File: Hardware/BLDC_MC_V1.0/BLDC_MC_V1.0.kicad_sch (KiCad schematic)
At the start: 0 parts

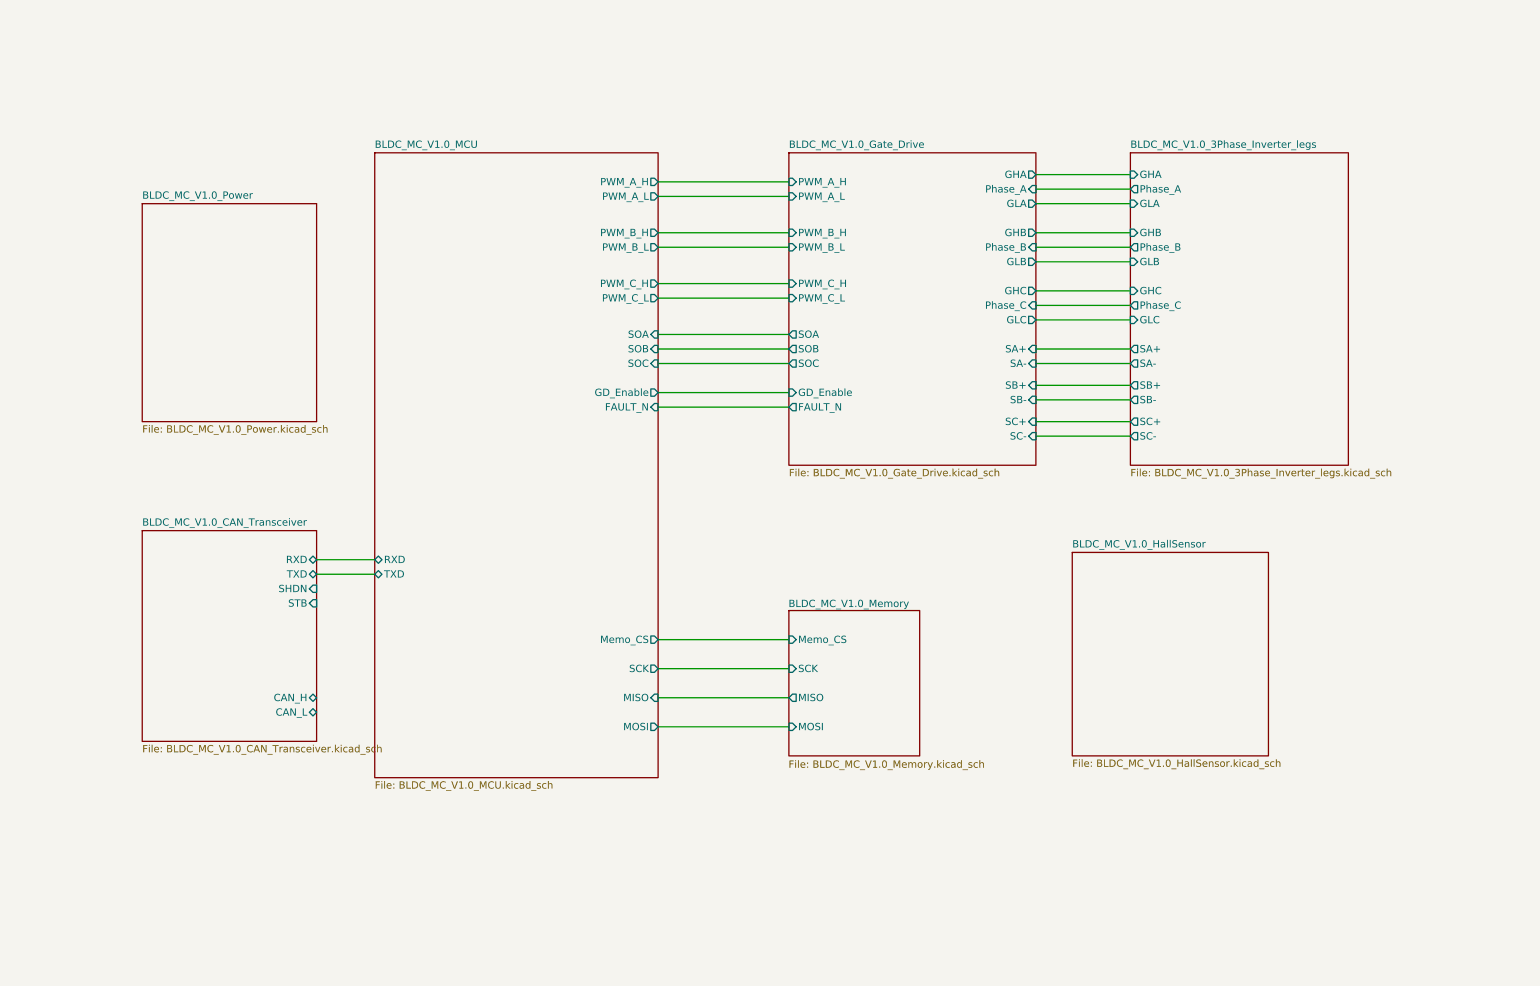
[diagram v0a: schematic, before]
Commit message: Edit the sch of the project by adding the hall sensor sheet and interface with the MCU sheet and annotate the components in memory sheet
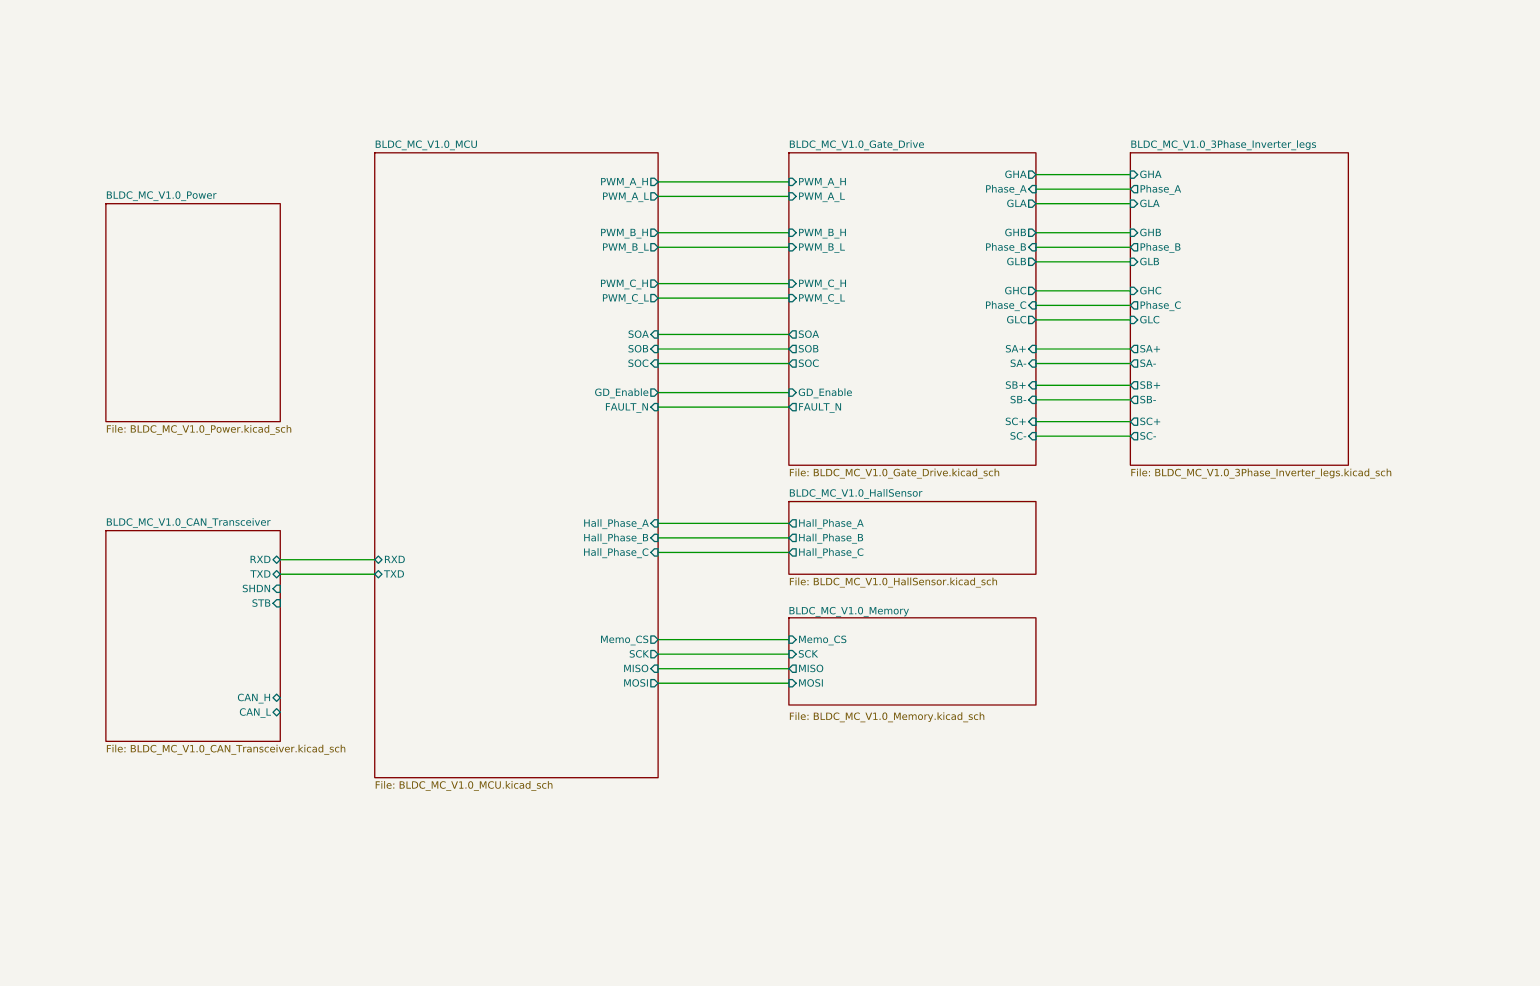
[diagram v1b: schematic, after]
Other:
- sheet BLDC_MC_V1.0_HallSensor ports: added Hall_Phase_A, Hall_Phase_B, Hall_Phase_C; removed none
- sheet BLDC_MC_V1.0_MCU ports: added Hall_Phase_A, Hall_Phase_B, Hall_Phase_C; removed none
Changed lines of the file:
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@@
 	(wire
 		(pts
-			(xy 77.47 115.57) (xy 87.63 115.57)
+			(xy 137.16 134.62) (xy 160.02 134.62)
+		)
+		(stroke
+			(width 0)
+			(type default)
+		)
+	)
+	(wire
+		(pts
+			(xy 137.16 111.76) (xy 160.02 111.76)
+		)
+		(stroke
+			(width 0)
+			(type default)
+		)
+	)
+	(wire
+		(pts
+			(xy 71.12 115.57) (xy 87.63 115.57)
 		)
 		(stroke
@@
 	(wire
 		(pts
-			(xy 77.47 118.11) (xy 87.63 118.11)
+			(xy 71.12 118.11) (xy 87.63 118.11)
 		)
 		(stroke
@@
 	(wire
 		(pts
-			(xy 137.16 134.62) (xy 160.02 134.62)
-		)
-		(stroke
-			(width 0)
-			(type default)
-		)
-	)
-	(wire
-		(pts
 			(xy 203.2 68.58) (xy 219.71 68.58)
 		)
@@
 	(wire
 		(pts
+			(xy 137.16 132.08) (xy 160.02 132.08)
+		)
+		(stroke
+			(width 0)
+			(type default)
+		)
+	)
+	(wire
+		(pts
 			(xy 203.2 93.98) (xy 219.71 93.98)
 		)
@@
 	(wire
 		(pts
+			(xy 137.16 109.22) (xy 160.02 109.22)
+		)
+		(stroke
+			(width 0)
+			(type default)
+		)
+	)
+	(wire
+		(pts
 			(xy 137.16 60.96) (xy 160.02 60.96)
 		)
@@
 	(wire
 		(pts
+			(xy 137.16 129.54) (xy 160.02 129.54)
+		)
+		(stroke
+			(width 0)
+			(type default)
+		)
+	)
+	(wire
+		(pts
 			(xy 203.2 78.74) (xy 219.71 78.74)
 		)
@@
 	(wire
 		(pts
-			(xy 137.16 144.78) (xy 160.02 144.78)
-		)
-		(stroke
-			(width 0)
-			(type default)
-		)
-	)
-	(wire
-		(pts
-			(xy 137.16 139.7) (xy 160.02 139.7)
+			(xy 137.16 114.3) (xy 160.02 114.3)
 		)
 		(stroke
@@
 	(wire
 		(pts
+			(xy 137.16 137.16) (xy 160.02 137.16)
+		)
+		(stroke
+			(width 0)
+			(type default)
+		)
+	)
+	(wire
+		(pts
 			(xy 137.16 52.07) (xy 160.02 52.07)
 		)
@@
 	(wire
 		(pts
-			(xy 137.16 129.54) (xy 160.02 129.54)
-		)
-		(stroke
-			(width 0)
-			(type default)
-		)
-	)
-	(wire
-		(pts
 			(xy 203.2 58.42) (xy 219.71 58.42)
 		)
@@
 	)
 	(sheet
-		(at 46.99 110.49)
+		(at 40.64 110.49)
 		(size 30.48 36.83)
 		(exclude_from_sim no)
@@
 		)
 		(property "Sheetname" "BLDC_MC_V1.0_CAN_Transceiver"
-			(at 46.99 109.7784 0)
+			(at 40.64 109.7784 0)
 			(effects
 				(font
@@
 		)
 		(property "Sheetfile" "BLDC_MC_V1.0_CAN_Transceiver.kicad_sch"
-			(at 46.99 147.9046 0)
+			(at 40.64 147.9046 0)
 			(effects
 				(font
@@
 		)
 		(pin "CAN_L" bidirectional
-			(at 77.47 142.24 0)
+			(at 71.12 142.24 0)
 			(effects
 				(font
@@
 		)
 		(pin "CAN_H" bidirectional
-			(at 77.47 139.7 0)
+			(at 71.12 139.7 0)
 			(effects
 				(font
@@
 		)
 		(pin "RXD" bidirectional
-			(at 77.47 115.57 0)
+			(at 71.12 115.57 0)
 			(effects
 				(font
@@
 		)
 		(pin "TXD" bidirectional
-			(at 77.47 118.11 0)
+			(at 71.12 118.11 0)
 			(effects
 				(font
@@
 		)
 		(pin "SHDN" input
-			(at 77.47 120.65 0)
+			(at 71.12 120.65 0)
 			(effects
 				(font
@@
 		)
 		(pin "STB" input
-			(at 77.47 123.19 0)
+			(at 71.12 123.19 0)
 			(effects
 				(font
@@
 		)
 		(pin "SCK" output
+			(at 137.16 132.08 0)
+			(effects
+				(font
+					(size 1.27 1.27)
+				)
+				(justify right)
+			)
+		)
+		(pin "MISO" input
 			(at 137.16 134.62 0)
 			(effects
@@
 			)
 		)
-		(pin "MISO" input
-			(at 137.16 139.7 0)
-			(effects
-				(font
-					(size 1.27 1.27)
-				)
-				(justify right)
-			)
-		)
 		(pin "MOSI" output
-			(at 137.16 144.78 0)
+			(at 137.16 137.16 0)
 			(effects
 				(font
@@
 		(pin "PWM_B_L" output
 			(at 137.16 60.96 0)
+			(effects
+				(font
+					(size 1.27 1.27)
+				)
+				(justify right)
+			)
+		)
+		(pin "Hall_Phase_A" input
+			(at 137.16 109.22 0)
+			(effects
+				(font
+					(size 1.27 1.27)
+				)
+				(justify right)
+			)
+		)
+		(pin "Hall_Phase_C" input
+			(at 137.16 114.3 0)
+			(effects
+				(font
+					(size 1.27 1.27)
+				)
+				(justify right)
+			)
+		)
+		(pin "Hall_Phase_B" input
+			(at 137.16 111.76 0)
 			(effects
 				(font
@@
 	)
 	(sheet
-		(at 160.02 124.46)
-		(size 22.86 25.4)
+		(at 160.02 125.73)
+		(size 43.18 15.24)
 		(exclude_from_sim no)
 		(in_bom yes)
@@
 		)
 		(property "Sheetname" "BLDC_MC_V1.0_Memory"
-			(at 159.9543 124.0001 0)
+			(at 159.9543 125.2701 0)
 			(effects
 				(font
@@
 		)
 		(property "Sheetfile" "BLDC_MC_V1.0_Memory.kicad_sch"
-			(at 159.9543 150.6044 0)
+			(at 160.02 142.24 0)
 			(effects
 				(font
@@
 		)
 		(pin "MOSI" input
-			(at 160.02 144.78 180)
+			(at 160.02 137.16 180)
 			(effects
 				(font
@@
 		)
 		(pin "SCK" input
-			(at 160.02 134.62 180)
+			(at 160.02 132.08 180)
 			(effects
 				(font
@@
 		)
 		(pin "MISO" output
-			(at 160.02 139.7 180)
+			(at 160.02 134.62 180)
 			(effects
 				(font
@@
 	)
 	(sheet
-		(at 209.55 114.3)
-		(size 34.29 35.56)
+		(at 160.02 105.41)
+		(size 43.18 12.7)
 		(exclude_from_sim no)
 		(in_bom yes)
@@
 		)
 		(property "Sheetname" "BLDC_MC_V1.0_HallSensor"
-			(at 209.55 113.5884 0)
+			(at 160.02 104.6984 0)
 			(effects
 				(font
@@
 		)
 		(property "Sheetfile" "BLDC_MC_V1.0_HallSensor.kicad_sch"
-			(at 209.55 150.4446 0)
+			(at 160.02 118.6946 0)
 			(effects
 				(font
@@
 				)
 				(justify left top)
+			)
+		)
+		(pin "Hall_Phase_B" output
+			(at 160.02 111.76 180)
+			(effects
+				(font
+					(size 1.27 1.27)
+				)
+				(justify left)
+			)
+		)
+		(pin "Hall_Phase_A" output
+			(at 160.02 109.22 180)
+			(effects
+				(font
+					(size 1.27 1.27)
+				)
+				(justify left)
+			)
+		)
+		(pin "Hall_Phase_C" output
+			(at 160.02 114.3 180)
+			(effects
+				(font
+					(size 1.27 1.27)
+				)
+				(justify left)
 			)
 		)
@@
 	)
 	(sheet
-		(at 46.99 53.34)
+		(at 40.64 53.34)
 		(size 30.48 38.1)
 		(exclude_from_sim no)
@@
 		)
 		(property "Sheetname" "BLDC_MC_V1.0_Power"
-			(at 46.99 52.6284 0)
+			(at 40.64 52.6284 0)
 			(effects
 				(font
@@
 		)
 		(property "Sheetfile" "BLDC_MC_V1.0_Power.kicad_sch"
-			(at 46.99 92.0246 0)
-			(effects
-				(font
+			(at 40.64 92.0246 0)
+			(effects
+				(font

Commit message: Add voltage sensor to measure the 3 phase voltage of inverter bridge
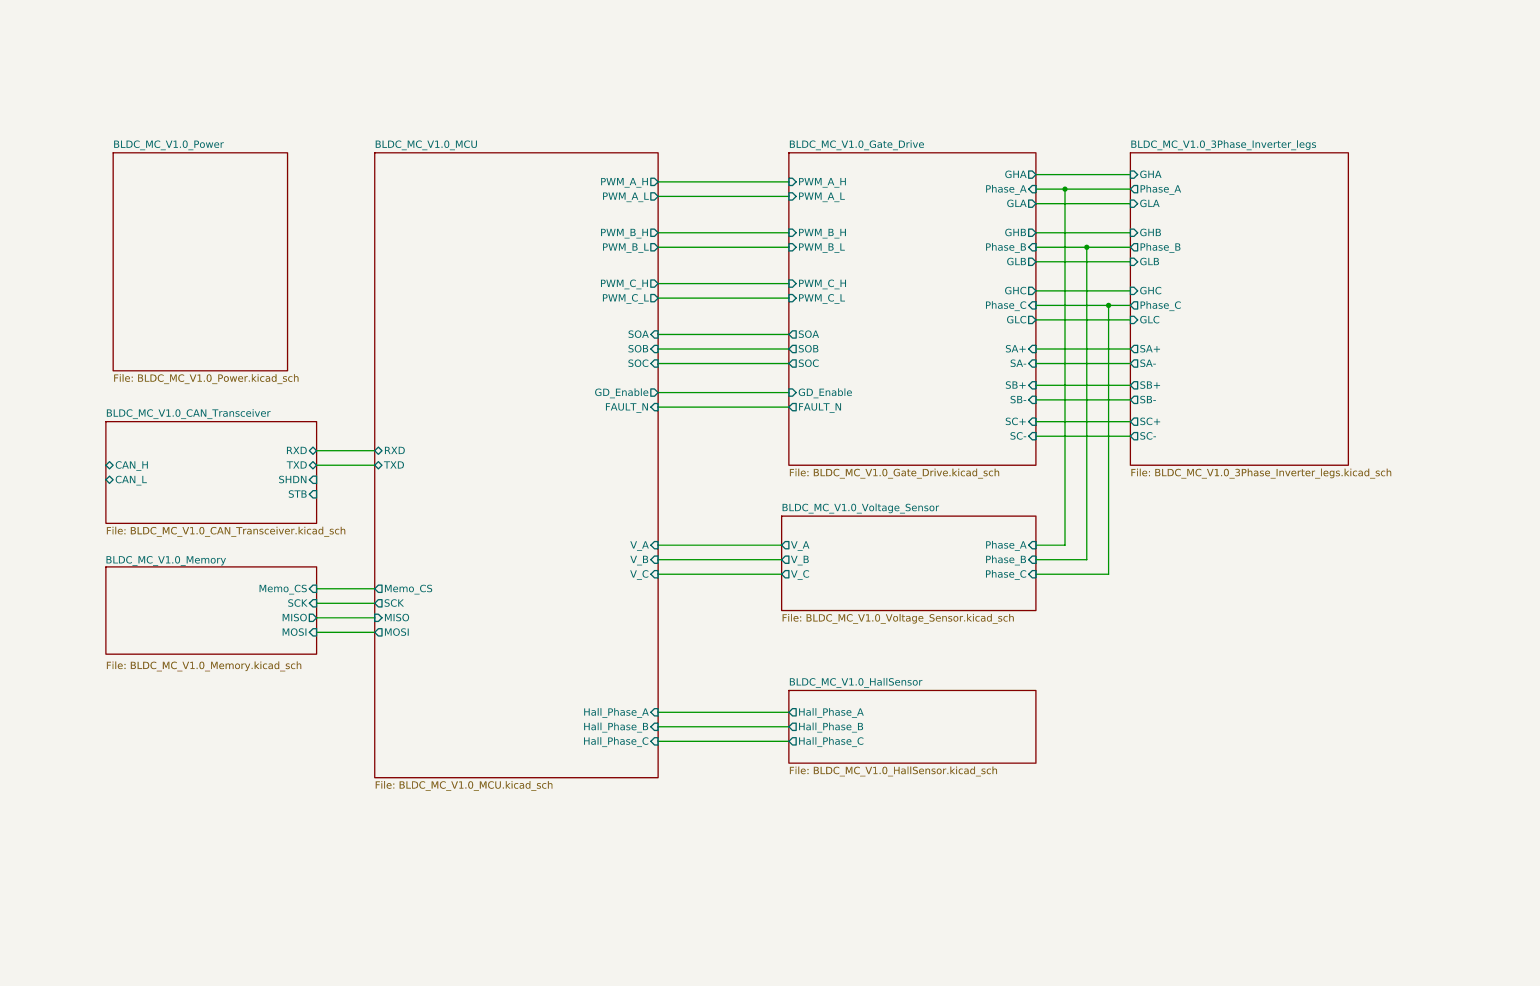
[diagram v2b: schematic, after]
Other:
- added sheet BLDC_MC_V1.0_Voltage_Sensor (BLDC_MC_V1.0_Voltage_Sensor.kicad_sch)
- sheet BLDC_MC_V1.0_MCU ports: added V_A, V_B, V_C; removed none
